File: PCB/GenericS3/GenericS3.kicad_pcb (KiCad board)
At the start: 2 copper layers, 70 x 70 mm, 69 parts, among them J1 USB-C-Socket-V, J4 DC, P1 33, P10 42, P11 45, P12 46, P13 47, P14 48, P15 18, P16 19, P17 14, P18 15, P19 16, P2 34, P20 17, P21 6, P22 7, P23 8, P24 9, P25 20, P26 10, P27 11, P28 12, P29 13, P3 35, P30 1, P31 2, P32 3, P33 4, P34 5, P35 21, P36 43, P37 44, P38 0, P39 ⏚, P4 36, P40 ⏚, P41 ⏚, P42 ⏚, P43 +, P44 +, P45 +, P46 +, P5 37, P6 38, P7 39, P8 40, P9 41, U2 ESP32-S3-MINI-1, U3 TPS562243

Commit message: Added diode
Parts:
- added D2: DKS22, RevK:D_SOD-123L, F.Cu at (114.8, 103.8)
- D1: value D -> DKS22; footprint RevK:D_SOD-123 -> RevK:D_SOD-123L
- moved J4 0.31 mm to (119.8, 107.1)
- moved D1 0.30 mm to (116.5, 94.1)
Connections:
- J4 pad 2: DC -> Net-(D2-A)
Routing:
- net Net-(D2-A): track 0.00 -> 18.5 mm
- net DC: track 28.8 -> 18.4 mm
- net SW: track 18.3 -> 16.2 mm
- net GND: vias 28 -> 22
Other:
- board text added: "ESP32-S3"

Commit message: Change reg
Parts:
- D1, D2: footprint RevK:D_SOD-123L -> RevK:D_SOD-123FL
- U3: value TPS562243 -> TPS562246
- moved J1 0.50 mm to (119.0, 91.0)
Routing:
- net GND: track 9.15 -> 6.54 mm

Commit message: Library update
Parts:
- added C2: 22uF 25V, RevK:C_0805, F.Cu at (114.8, 111.8)
- added C4: 22uF 25V, RevK:C_0805, F.Cu at (114.8, 100.8)
- C15: value 47uF 6V -> 47uF; footprint RevK:C_0805 -> RevK:C_0805_Tant
- moved C17 4.30 mm to (114.8, 104.0), turned to 90 degrees
- moved D2 4.10 mm to (114.7, 107.9)
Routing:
- net DC: track 18.4 -> 24.4 mm
- net Net-(D2-A): track 18.5 -> 20.8 mm
- net +3.3V: track 119.1 -> 117.2 mm
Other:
- board text removed: "ESP32-S3"

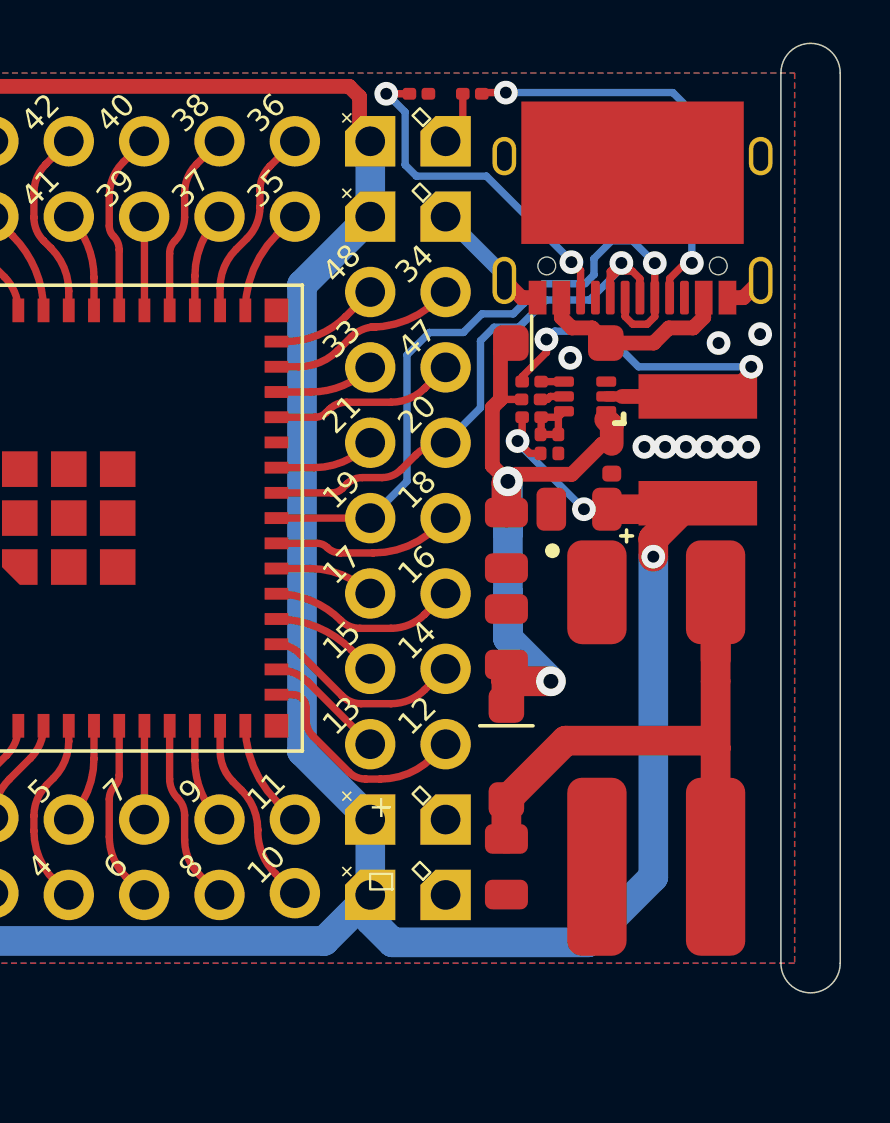
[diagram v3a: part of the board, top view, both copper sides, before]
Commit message: More caps
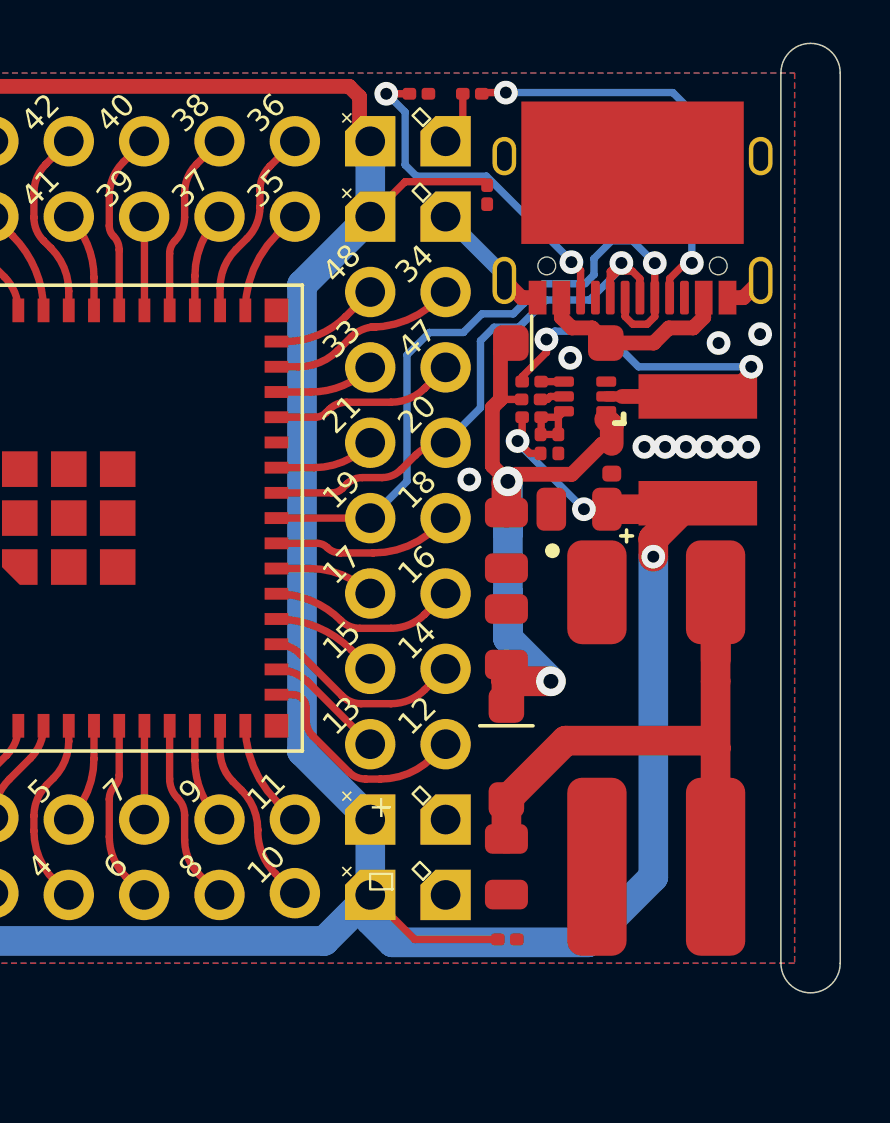
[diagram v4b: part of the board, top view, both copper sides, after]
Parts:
- added C6: 100nF, RevK:C_0201, F.Cu at (114.8, 114.2)
- added C7: 100nF, RevK:C_0201, F.Cu at (114.1, 89.1)
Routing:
- net +3.3V: track 117.2 -> 126.6 mm
- net GND: vias 22 -> 23

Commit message: Latest tweaks
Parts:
- added C8: 100nF, RevK:C_0201, F.Cu at (123.3, 100.9)
- added C9: 100nF, RevK:C_0201, F.Cu at (109.4, 85.7)
- moved C1 0.26 mm to (93.2, 108.2)
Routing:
- net +3.3V: track 126.6 -> 154.5 mm, vias 4 -> 5
- net GND: vias 23 -> 26

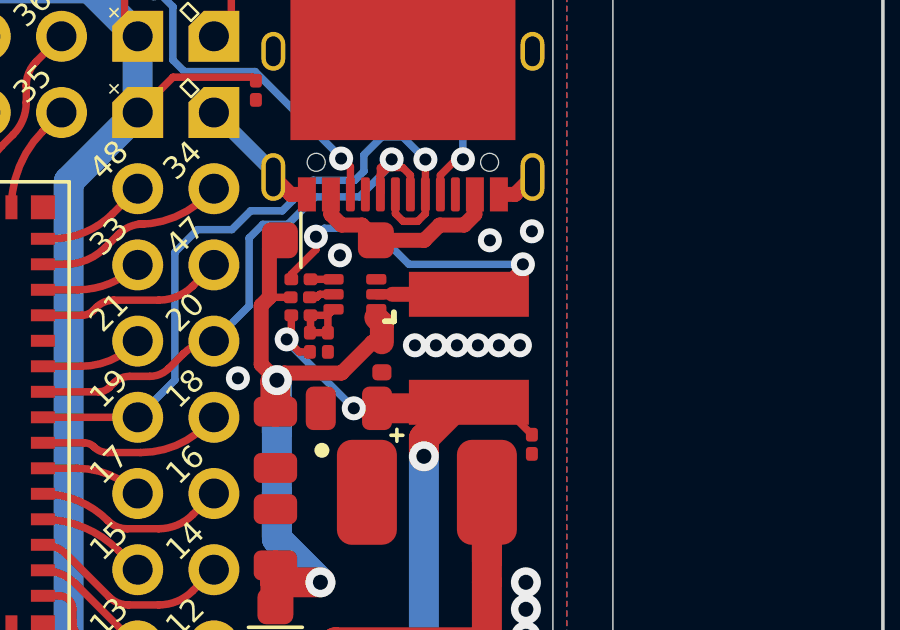
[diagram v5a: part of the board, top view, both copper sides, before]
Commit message: More caps, and change to ceramic
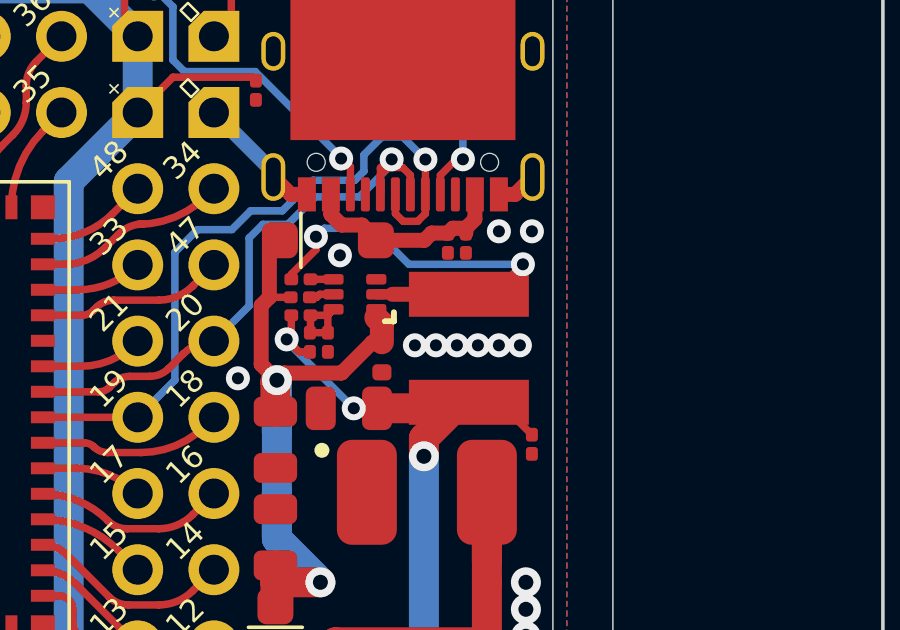
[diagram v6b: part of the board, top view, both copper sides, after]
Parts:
- removed C15: 47uF, RevK:C_0805_Tant
- added C10: 100nF, RevK:C_0201, F.Cu at (120.5, 94.2)
- added C11: 100nF, RevK:C_0201, F.Cu at (121.1, 94.2)
- added C5: 47uF 6V, RevK:C_0805, F.Cu at (117.2, 99.7)

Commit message: Tweak layout a bit
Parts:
- D1, D2: value DKS22 -> DKS34
